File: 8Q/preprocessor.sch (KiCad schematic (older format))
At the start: 0 parts

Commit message: modified:   8Q/8Q-cache.lib 	modified:   8Q/8Q.sch 	modified:   8Q/8_qp_io.sch 	new file:   8Q/RAM.sch 	deleted:    8Q/_saved_RAM.sch 	modified:   8Q/cpu.sch 	modified:   8Q/cpu_power.sch 	modified:   8Q/power.sch 	modified:   8Q/preprocessor.sch 	modified:   8Q/qpower.sch 	modified:   8Q/qpu.sch 	new file:   8q.dia 	modified:   README.md 	new file:   docs/source/imgs/8q.png
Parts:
- added U?: S5933_PQ160, Package_QFP:PQFP-160_28x28mm_P0.65mm, symbol Interface:S5933_PQ160
- added U?: IS42S16400J-xC, Package_SO:TSOP-II-54_10.16x22.22mm_P0.8mm, symbol Memory_RAM:IS42S16400J-xC
- added U?: STM32F429BITx, Package_QFP:LQFP-208_28x28mm_P0.5mm, symbol MCU_ST_STM32F4:STM32F429BITx
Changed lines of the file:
@@
 EELAYER 26 0
 EELAYER END
-$Descr A4 11693 8268
+$Descr A1 33110 23386
 encoding utf-8
-Sheet 5 8
+Sheet 6 9
 Title "8Q Quantum Computer"
 Date "2020-06-29"
@@
 Comment4 "Development Schematics"
 $EndDescr
+$Comp
+L Interface:S5933_PQ160 U?
+U 1 1 5F32A775
+P 5050 6350
+F 0 "U?" H 5050 10928 50  0000 C CNN
+F 1 "S5933_PQ160" H 5050 10837 50  0000 C CNN
+F 2 "Package_QFP:PQFP-160_28x28mm_P0.65mm" H 5050 1850 50  0001 C CNN
+F 3 "http://datasheet.datasheetarchive.com/originals/distributors/Datasheets-35/DSA-684194.pdf" H 5050 6350 50  0001 C CNN
+	1    5050 6350
+	1    0    0    -1
+$EndComp
+$Comp
+L Memory_RAM:IS42S16400J-xC U?
+U 1 1 5F32A907
+P 12000 3950
+F 0 "U?" H 12000 5528 50  0000 C CNN
+F 1 "IS42S16400J-xC" H 12000 5437 50  0000 C CNN
+F 2 "Package_SO:TSOP-II-54_10.16x22.22mm_P0.8mm" H 12000 3950 50  0001 C CNN
+F 3 "http://www.issi.com/WW/pdf/42-45S16400J.pdf" H 11400 5200 50  0001 C CNN
+	1    12000 3950
+	1    0    0    -1
+$EndComp
+$Comp
+L MCU_ST_STM32F4:STM32F429BITx U?
+U 1 1 5F32AB85
+P 17250 8450
+F 0 "U?" H 17200 3064 50  0000 C CNN
+F 1 "STM32F429BITx" H 17200 2973 50  0000 C CNN
+F 2 "Package_QFP:LQFP-208_28x28mm_P0.5mm" H 15950 3350 50  0001 R CNN
+F 3 "http://www.st.com/st-web-ui/static/active/en/resource/technical/document/datasheet/DM00071990.pdf" H 17250 8450 50  0001 C CNN
+	1    17250 8450
+	1    0    0    -1
+$EndComp
 $EndSCHEMATC

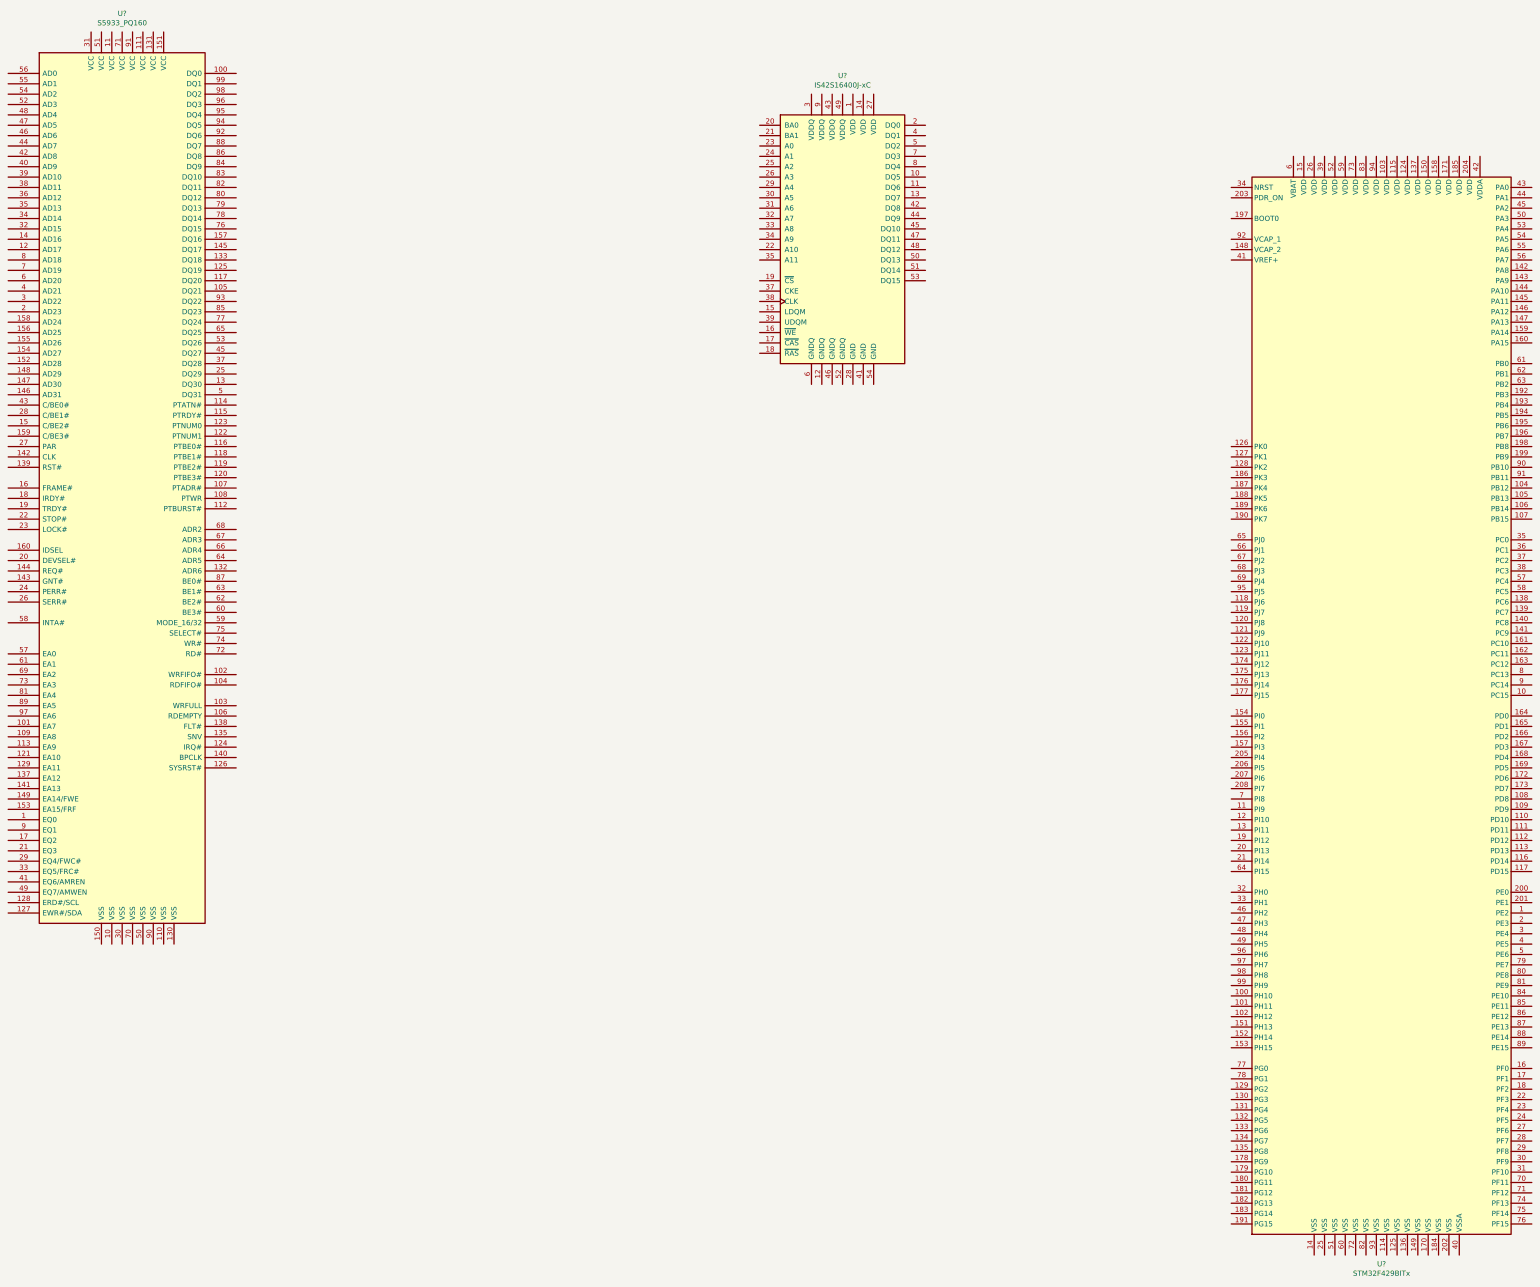
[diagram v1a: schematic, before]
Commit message: modified:   8Q/8Q-cache.lib 	modified:   8Q/8Q.sch 	modified:   8Q/8_qp_io.sch 	modified:   8Q/RAM.sch 	new file:   8Q/control_logic.sch 	modified:   8Q/cpu.sch 	modified:   8Q/cpu_power.sch 	new file:   8Q/inorder.sch 	new file:   8Q/instruction_bus.sch 	new file:   8Q/output_cache.sch 	modified:   8Q/power.sch 	modified:   8Q/preprocessor.sch 	modified:   8Q/qpower.sch 	modified:   8Q/qpu.sch 	new file:   Controller.md 	modified:   QCore.md 	new file:   QPU_Operation.md 	new file:   docs/source/imgs/Screenshot from 2020-07-07 18-04-51.png 	new file:   tools/photon_birth_death.py 	new file:   tools/processor.py
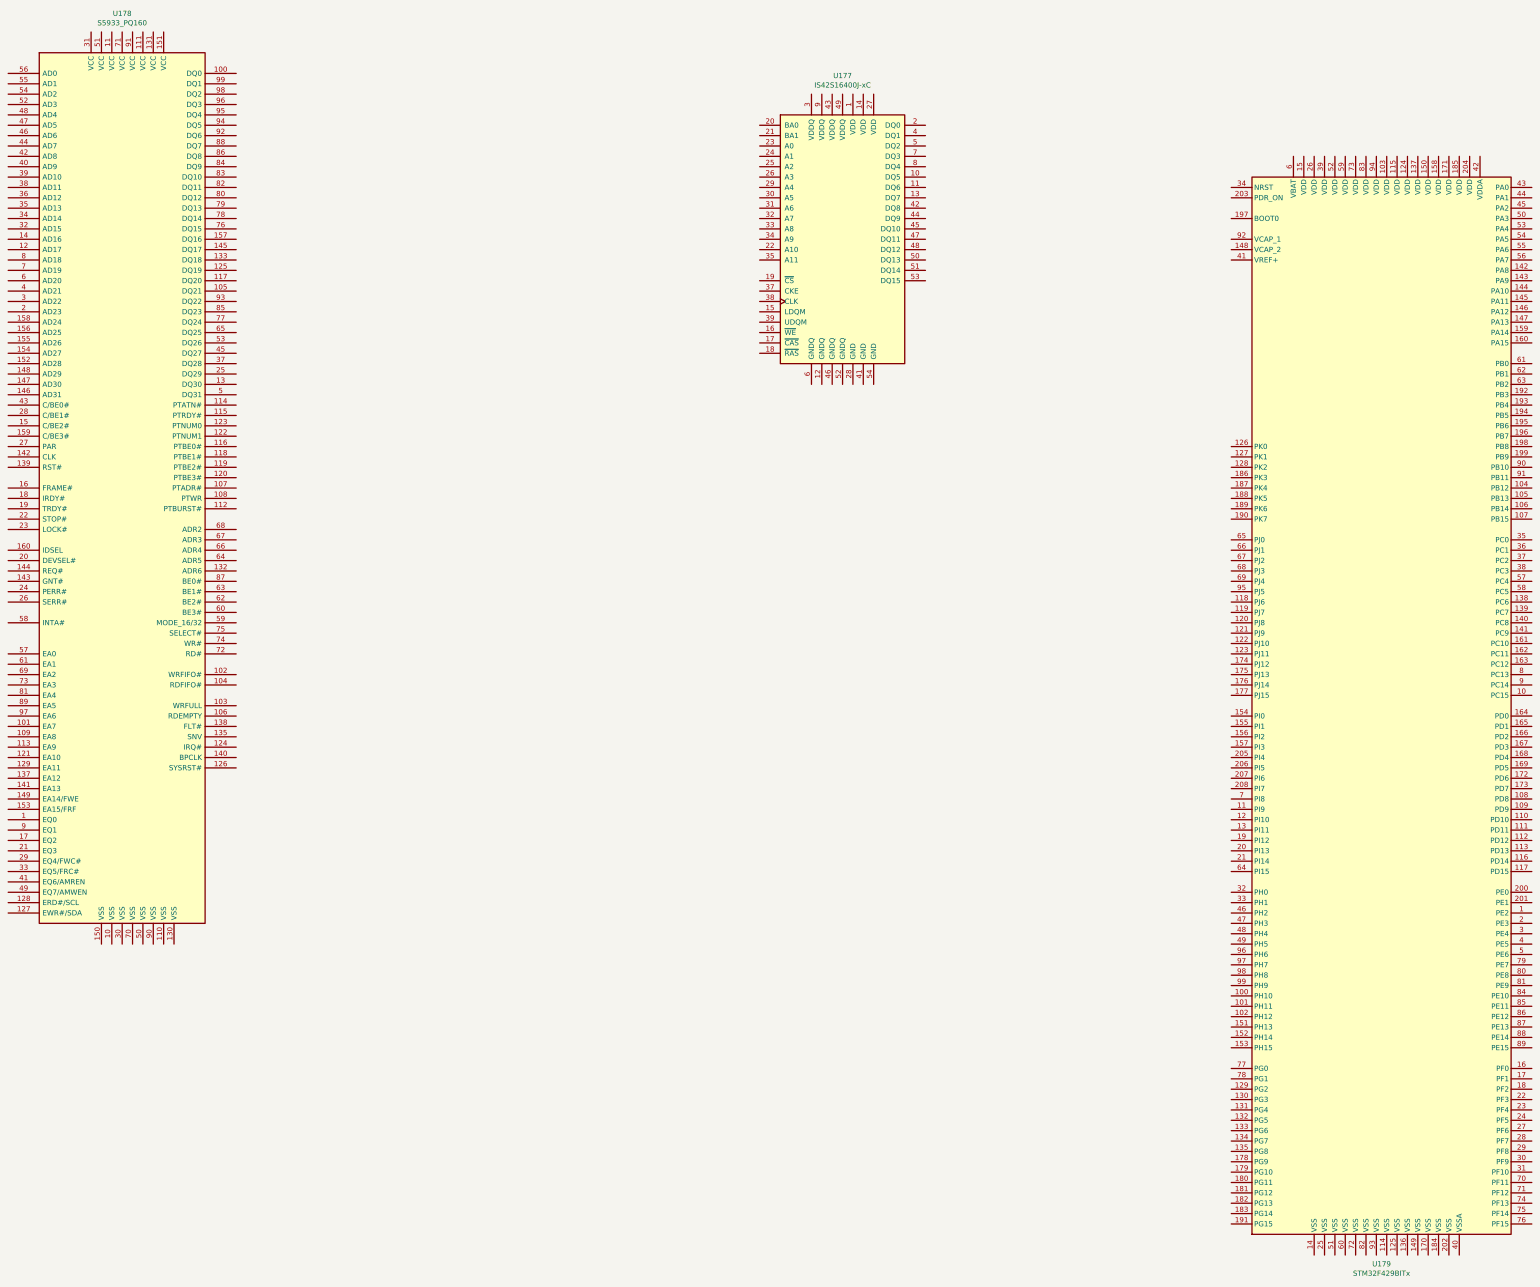
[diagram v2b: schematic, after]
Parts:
- gave numbers to parts that had none: 3
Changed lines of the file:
@@
 $Descr A1 33110 23386
 encoding utf-8
-Sheet 6 9
+Sheet 6 13
 Title "8Q Quantum Computer"
 Date "2020-06-29"
@@
 $EndDescr
 $Comp
-L Interface:S5933_PQ160 U?
+L Interface:S5933_PQ160 U178
 U 1 1 5F32A775
 P 5050 6350
-F 0 "U?" H 5050 10928 50  0000 C CNN
+F 0 "U178" H 5050 10928 50  0000 C CNN
 F 1 "S5933_PQ160" H 5050 10837 50  0000 C CNN
 F 2 "Package_QFP:PQFP-160_28x28mm_P0.65mm" H 5050 1850 50  0001 C CNN
@@
 $EndComp
 $Comp
-L Memory_RAM:IS42S16400J-xC U?
+L Memory_RAM:IS42S16400J-xC U177
 U 1 1 5F32A907
 P 12000 3950
-F 0 "U?" H 12000 5528 50  0000 C CNN
+F 0 "U177" H 12000 5528 50  0000 C CNN
 F 1 "IS42S16400J-xC" H 12000 5437 50  0000 C CNN
 F 2 "Package_SO:TSOP-II-54_10.16x22.22mm_P0.8mm" H 12000 3950 50  0001 C CNN
@@
 $EndComp
 $Comp
-L MCU_ST_STM32F4:STM32F429BITx U?
+L MCU_ST_STM32F4:STM32F429BITx U179
 U 1 1 5F32AB85
 P 17250 8450
-F 0 "U?" H 17200 3064 50  0000 C CNN
+F 0 "U179" H 17200 3064 50  0000 C CNN
 F 1 "STM32F429BITx" H 17200 2973 50  0000 C CNN
 F 2 "Package_QFP:LQFP-208_28x28mm_P0.5mm" H 15950 3350 50  0001 R CNN
